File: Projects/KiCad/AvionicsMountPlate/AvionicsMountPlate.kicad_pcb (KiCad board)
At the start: 2 copper layers, 140 x 140 mm, 29 parts

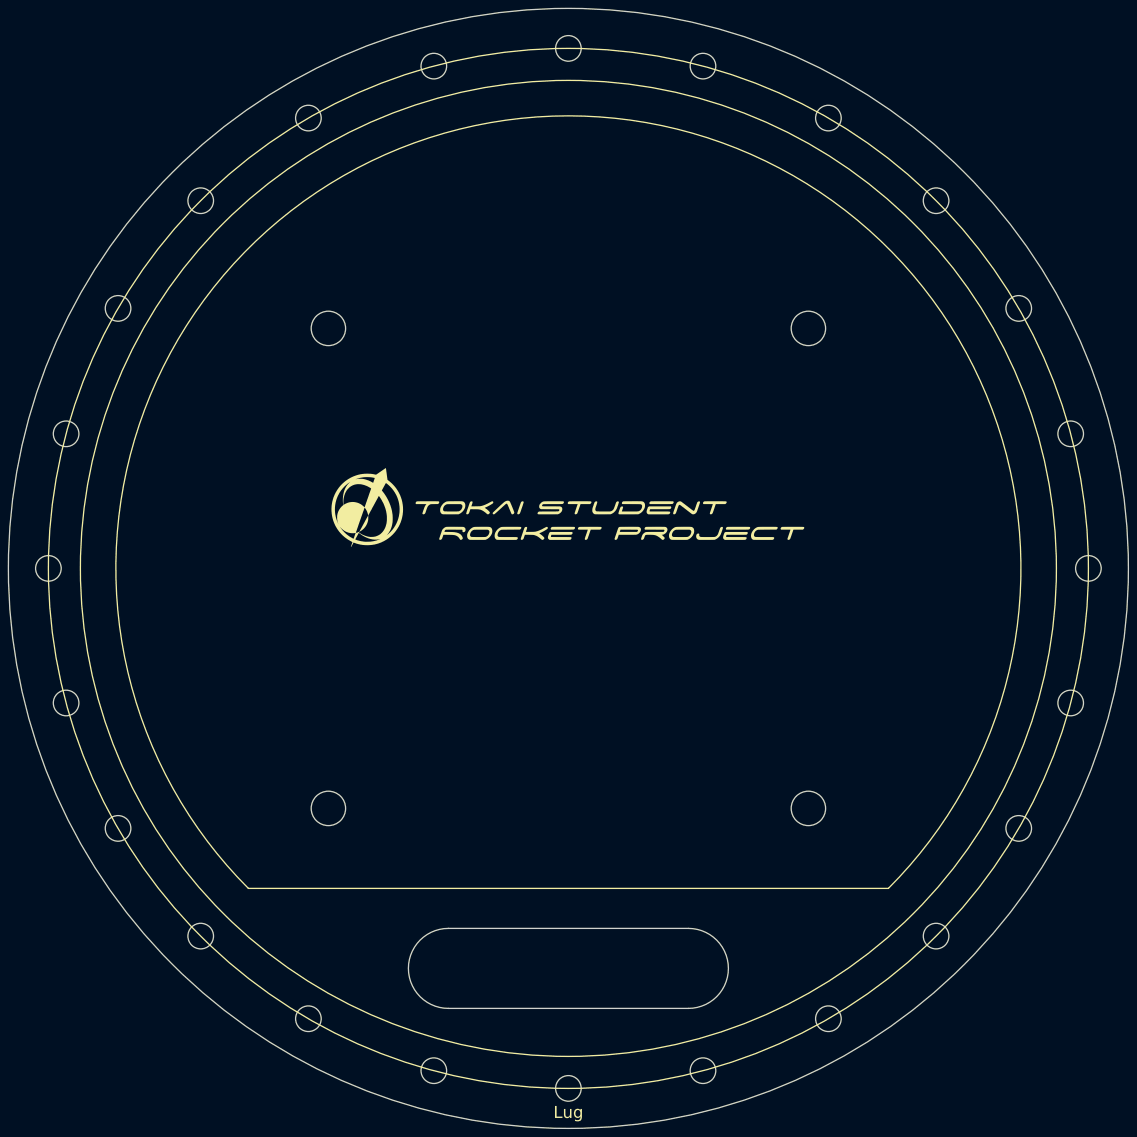
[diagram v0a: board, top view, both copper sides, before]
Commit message: 計器マウントプレートの穴径をタカチのケーブルグランドにあわせて修正
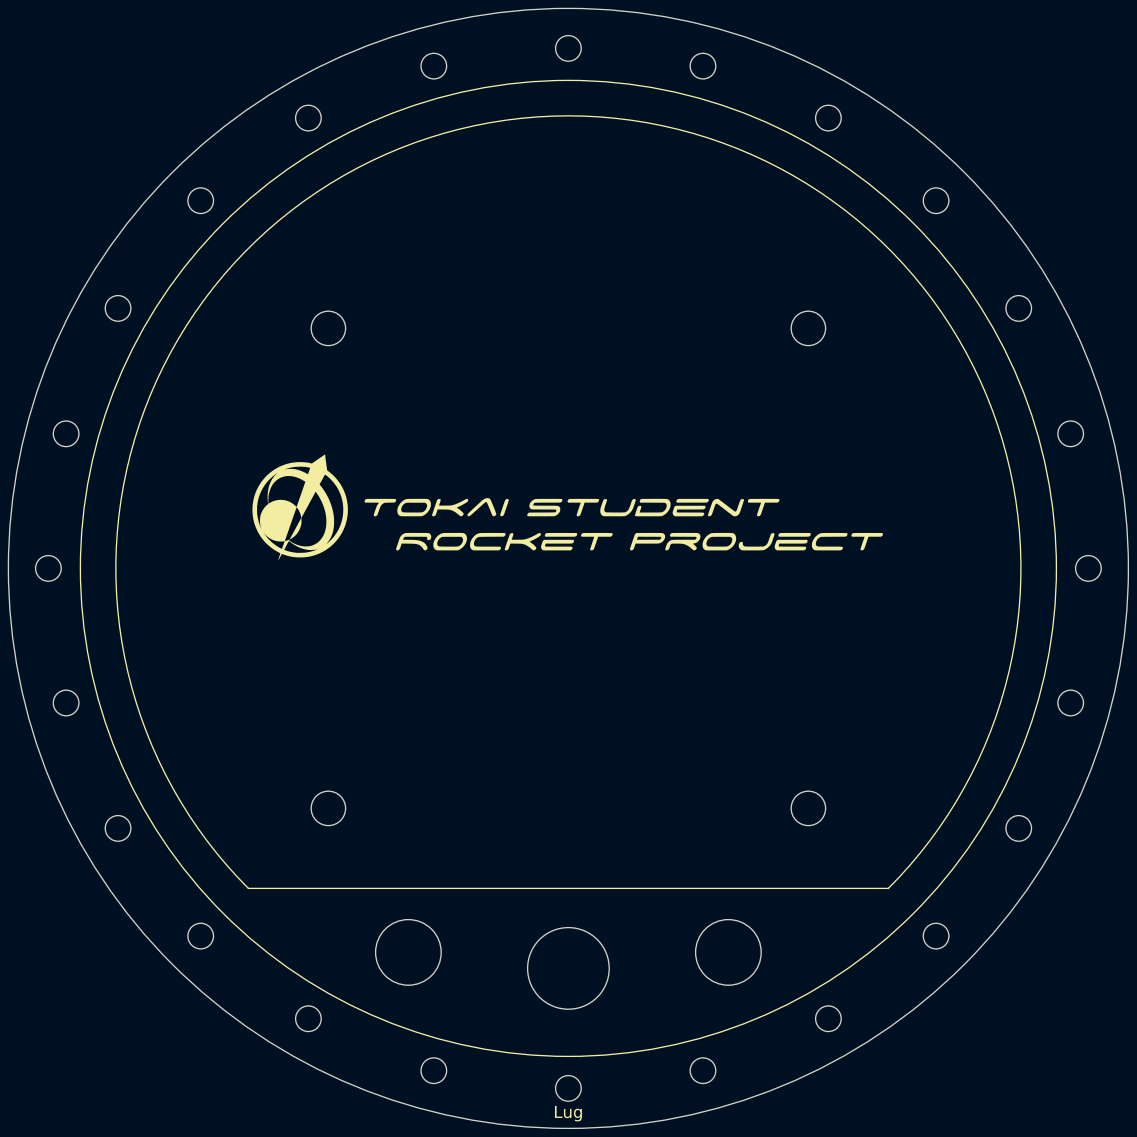
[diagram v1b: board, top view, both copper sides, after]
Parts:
- added REF**: MountingHole_8.2mm, MountingHole:MountingHole_6mm, F.Cu at (-20.0, 48.0)
- added REF**: MountingHole_10.2mm, MountingHole:MountingHole_8.4mm_M8, F.Cu at (0.00, 50.0)
- added REF**: MountingHole_8.2mm, MountingHole:MountingHole_6mm, F.Cu at (20.0, 48.0)
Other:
- outline, holes or cut-outs redrawn

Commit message: 原点を設定
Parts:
- moved REF** 173.3 mm to (103.7, 133.3)
- moved REF** 173.3 mm to (86.8, 70.6)
- moved REF** 173.3 mm to (119.6, 57.4)
- moved REF** 173.3 mm to (195.6, 41.4)
- moved REF** 173.3 mm to (103.7, 41.4)
- moved REF** 173.3 mm to (195.6, 133.3)
- moved REF** 173.3 mm to (132.8, 150.2)
- moved REF** 173.3 mm to (93.3, 119.9)
- moved REF** 173.3 mm to (117.1, 143.7)
- moved REF** 173.3 mm to (93.3, 54.9)
- moved REF** 173.3 mm to (117.1, 31.1)
- moved REF** 173.3 mm to (119.6, 117.4)
- moved REF** 173.3 mm to (84.6, 87.4)
- moved REF** 173.3 mm to (132.8, 24.6)
- moved REF** 173.3 mm to (86.8, 104.2)
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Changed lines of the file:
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@@
   (setup
     (pad_to_mask_clearance 0)
+    (aux_axis_origin 79.618059 17.388059)
+    (grid_origin 149.618059 87.388059)
     (pcbplotparams
       (layerselection 0x00010fc_ffffffff)
@@
   (net 0 "")
   (footprint "MountingHole:MountingHole_3.2mm_M3" (layer "F.Cu")
-    (at 56.291651 -32.5)
+    (at 205.90971 54.888059)
     (descr "Mounting Hole 3.2mm, no annular, M3")
     (tags "mounting hole 3.2mm no annular m3")
@@
   )
   (footprint "MountingHole:MountingHole_3.2mm_M3" (layer "F.Cu")
-    (at 45.961941 45.961941)
+    (at 195.58 133.35)
     (descr "Mounting Hole 3.2mm, no annular, M3")
     (tags "mounting hole 3.2mm no annular m3")
@@
   )
   (footprint "MountingHole:MountingHole_3.2mm_M3" (layer "F.Cu")
-    (at 16.823238 62.785179)
+    (at 166.441297 150.173238)
     (descr "Mounting Hole 3.2mm, no annular, M3")
     (tags "mounting hole 3.2mm no annular m3")
@@
   )
   (footprint "MountingHole:MountingHole_3.2mm_M3" (layer "F.Cu")
-    (at -65 0)
+    (at 84.618059 87.388059)
     (descr "Mounting Hole 3.2mm, no annular, M3")
     (tags "mounting hole 3.2mm no annular m3")
@@
   )
   (footprint "MountingHole:MountingHole_3.2mm_M3" (layer "F.Cu")
-    (at -16.823238 -62.785179)
+    (at 132.794821 24.60288)
     (descr "Mounting Hole 3.2mm, no annular, M3")
     (tags "mounting hole 3.2mm no annular m3")
@@
   )
   (footprint "MountingHole:MountingHole_3.2mm_M3" (layer "F.Cu")
-    (at 56.291651 32.5)
+    (at 205.90971 119.888059)
     (descr "Mounting Hole 3.2mm, no annular, M3")
     (tags "mounting hole 3.2mm no annular m3")
@@
   )
   (footprint "MountingHole:MountingHole_3.2mm_M3" (layer "F.Cu")
-    (at 16.823238 -62.785179)
+    (at 166.441297 24.60288)
     (descr "Mounting Hole 3.2mm, no annular, M3")
     (tags "mounting hole 3.2mm no annular m3")
@@
   )
   (footprint "MountingHole:MountingHole_3.2mm_M3" (layer "F.Cu")
-    (at -62.785179 16.823238)
+    (at 86.83288 104.211297)
     (descr "Mounting Hole 3.2mm, no annular, M3")
     (tags "mounting hole 3.2mm no annular m3")
@@
   )
   (footprint "MountingHole:MountingHole_3.2mm_M3" (layer "F.Cu")
-    (at 32.5 56.291651)
+    (at 182.118059 143.67971)
     (descr "Mounting Hole 3.2mm, no annular, M3")
     (tags "mounting hole 3.2mm no annular m3")
@@
   )
   (footprint "MountingHole:MountingHole_3.2mm_M3" (layer "F.Cu")
-    (at -45.961941 45.961941)
+    (at 103.656118 133.35)
     (descr "Mounting Hole 3.2mm, no annular, M3")
     (tags "mounting hole 3.2mm no annular m3")
@@
   )
   (footprint "MountingHole:MountingHole_3.2mm_M3" (layer "F.Cu")
-    (at 32.5 -56.291651)
+    (at 182.118059 31.096408)
     (descr "Mounting Hole 3.2mm, no annular, M3")
     (tags "mounting hole 3.2mm no annular m3")
@@
   )
   (footprint "MountingHole:MountingHole_3.2mm_M3" (layer "F.Cu")
-    (at -62.785179 -16.823238)
+    (at 86.83288 70.564821)
     (descr "Mounting Hole 3.2mm, no annular, M3")
     (tags "mounting hole 3.2mm no annular m3")
@@
   )
   (footprint "MountingHole:MountingHole_6mm" (layer "F.Cu")
-    (at -20 48)
+    (at 129.618059 135.388059)
     (descr "Mounting Hole 6mm, no annular")
     (tags "mounting hole 6mm no annular")
@@
   )
   (footprint "MountingHole:MountingHole_8.4mm_M8" (layer "F.Cu")
-    (at 0 50)
+    (at 149.618059 137.388059)
     (descr "Mounting Hole 8.4mm, no annular, M8")
     (tags "mounting hole 8.4mm no annular m8")
@@
   )
   (footprint "MountingHole:MountingHole_3.2mm_M3" (layer "F.Cu")
-    (at 62.785179 -16.823238)
+    (at 212.403238 70.564821)
     (descr "Mounting Hole 3.2mm, no annular, M3")
     (tags "mounting hole 3.2mm no annular m3")
@@
   )
   (footprint "MountingHole:MountingHole_4.3mm_M4" (layer "F.Cu")
-    (at -30 -30)
+    (at 119.618059 57.388059)
     (descr "Mounting Hole 4.3mm, no annular, M4")
     (tags "mounting hole 4.3mm no annular m4")
@@
   )
   (footprint "MountingHole:MountingHole_3.2mm_M3" (layer "F.Cu")
-    (at 45.961941 -45.961941)
+    (at 195.58 41.426118)
     (descr "Mounting Hole 3.2mm, no annular, M3")
     (tags "mounting hole 3.2mm no annular m3")
@@
   )
   (footprint "MountingHole:MountingHole_3.2mm_M3" (layer "F.Cu")
-    (at -45.961941 -45.961941)
+    (at 103.656118 41.426118)
     (descr "Mounting Hole 3.2mm, no annular, M3")
     (tags "mounting hole 3.2mm no annular m3")
@@
   )
   (footprint "MountingHole:MountingHole_4.3mm_M4" (layer "F.Cu")
-    (at 30 -30)
+    (at 179.618059 57.388059)
     (descr "Mounting Hole 4.3mm, no annular, M4")
     (tags "mounting hole 4.3mm no annular m4")
@@
   )
   (footprint "MountingHole:MountingHole_3.2mm_M3" (layer "F.Cu")
-    (at -16.823238 62.785179)
+    (at 132.794821 150.173238)
     (descr "Mounting Hole 3.2mm, no annular, M3")
     (tags "mounting hole 3.2mm no annular m3")
@@
   )
   (footprint "MountingHole:MountingHole_3.2mm_M3" (layer "F.Cu")
-    (at -56.291651 32.5)
+    (at 93.326408 119.888059)
     (descr "Mounting Hole 3.2mm, no annular, M3")
     (tags "mounting hole 3.2mm no annular m3")
@@
   )
   (footprint "MountingHole:MountingHole_3.2mm_M3" (layer "F.Cu")
-    (at -32.5 56.291651)
+    (at 117.118059 143.67971)
     (descr "Mounting Hole 3.2mm, no annular, M3")
     (tags "mounting hole 3.2mm no annular m3")
@@
   )
   (footprint "MountingHole:MountingHole_3.2mm_M3" (layer "F.Cu")
-    (at 0 -65)
+    (at 149.618059 22.388059)
     (descr "Mounting Hole 3.2mm, no annular, M3")
     (tags "mounting hole 3.2mm no annular m3")
@@
   )
   (footprint "MountingHole:MountingHole_3.2mm_M3" (layer "F.Cu")
-    (at 65 0)
+    (at 214.618059 87.388059)
     (descr "Mounting Hole 3.2mm, no annular, M3")
     (tags "mounting hole 3.2mm no annular m3")
@@
   )
   (footprint "MountingHole:MountingHole_3.2mm_M3" (layer "F.Cu")
-    (at -56.291651 -32.5)
+    (at 93.326408 54.888059)
     (descr "Mounting Hole 3.2mm, no annular, M3")
     (tags "mounting hole 3.2mm no annular m3")
@@
   )
   (footprint "MountingHole:MountingHole_6mm" (layer "F.Cu")
-    (at 20 48)
+    (at 169.618059 135.388059)
     (descr "Mounting Hole 6mm, no annular")
     (tags "mounting hole 6mm no annular")
@@
   )
   (footprint "MountingHole:MountingHole_3.2mm_M3" (layer "F.Cu")
-    (at -32.5 -56.291651)
+    (at 117.118059 31.096408)
     (descr "Mounting Hole 3.2mm, no annular, M3")
     (tags "mounting hole 3.2mm no annular m3")
@@
   )
   (footprint "MountingHole:MountingHole_4.3mm_M4" (layer "F.Cu")
-    (at -30 30)
+    (at 119.618059 117.388059)
     (descr "Mounting Hole 4.3mm, no annular, M4")
     (tags "mounting hole 4.3mm no annular m4")
@@
   )
   (footprint "MountingHole:MountingHole_4.3mm_M4" (layer "F.Cu")
-    (at 30 30)
+    (at 179.618059 117.388059)
     (descr "Mounting Hole 4.3mm, no annular, M4")
     (tags "mounting hole 4.3mm no annular m4")
@@
   )
   (footprint "MountingHole:MountingHole_3.2mm_M3" (layer "F.Cu")
-    (at 62.785179 16.823238)
+    (at 212.403238 104.211297)
     (descr "Mounting Hole 3.2mm, no annular, M3")
     (tags "mounting hole 3.2mm no annular m3")
@@
   )
   (footprint "LOGO" (layer "F.Cu")
-    (at 0 -7.5)
+    (at 149.618059 79.888059)
     (attr board_only exclude_from_pos_files exclude_from_bom)
     (fp_text reference "G***" (at 0 0) (layer "F.SilkS") hide
@@
   )
   (footprint "MountingHole:MountingHole_3.2mm_M3" (layer "F.Cu")
-    (at 0 65)
+    (at 149.618059 152.388059)
     (descr "Mounting Hole 3.2mm, no annular, M3")
     (tags "mounting hole 3.2mm no annular m3")
@@
     (pad "" np_thru_hole circle (at 0 0) (size 3.2 3.2) (drill 3.2) (layers "*.Cu" "*.Mask"))
   )
-  (gr_circle (center 0 0) (end 61 0)
+  (gr_circle (center 149.618059 87.388059) (end 210.618059 87.388059)
     (stroke (width 0.1) (type solid)) (fill none) (layer "F.SilkS"))
-  (gr_line (start -40 40) (end 40 40)
+  (gr_line (start 109.618059 127.388059) (end 189.618059 127.388059)
     (stroke (width 0.1) (type default)) (layer "F.SilkS"))
-  (gr_arc (start -40 40) (mid 0 -56.568542) (end 40 40)
+  (gr_arc (start 109.618059 127.388059) (mid 149.618059 30.819517) (end 189.618059 127.388059)
     (stroke (width 0.1) (type default)) (layer "F.SilkS"))
-  (gr_circle (center 0 0) (end 70 0)
+  (gr_circle (center 149.618059 87.388059) (end 219.618059 87.388059)
     (stroke (width 0.1) (type default)) (fill none) (layer "Edge.Cuts"))
-  (gr_text "Lug" (at 0 68) (layer "F.SilkS")
+  (gr_text "Lug" (at 149.618059 155.388059) (layer "F.SilkS")
     (effects (font (size 1.5 1.5) (thickness 0.15)))
   )
